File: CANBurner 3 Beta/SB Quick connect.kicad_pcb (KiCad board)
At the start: 2 copper layers, 33.8 x 30 mm, 9 parts

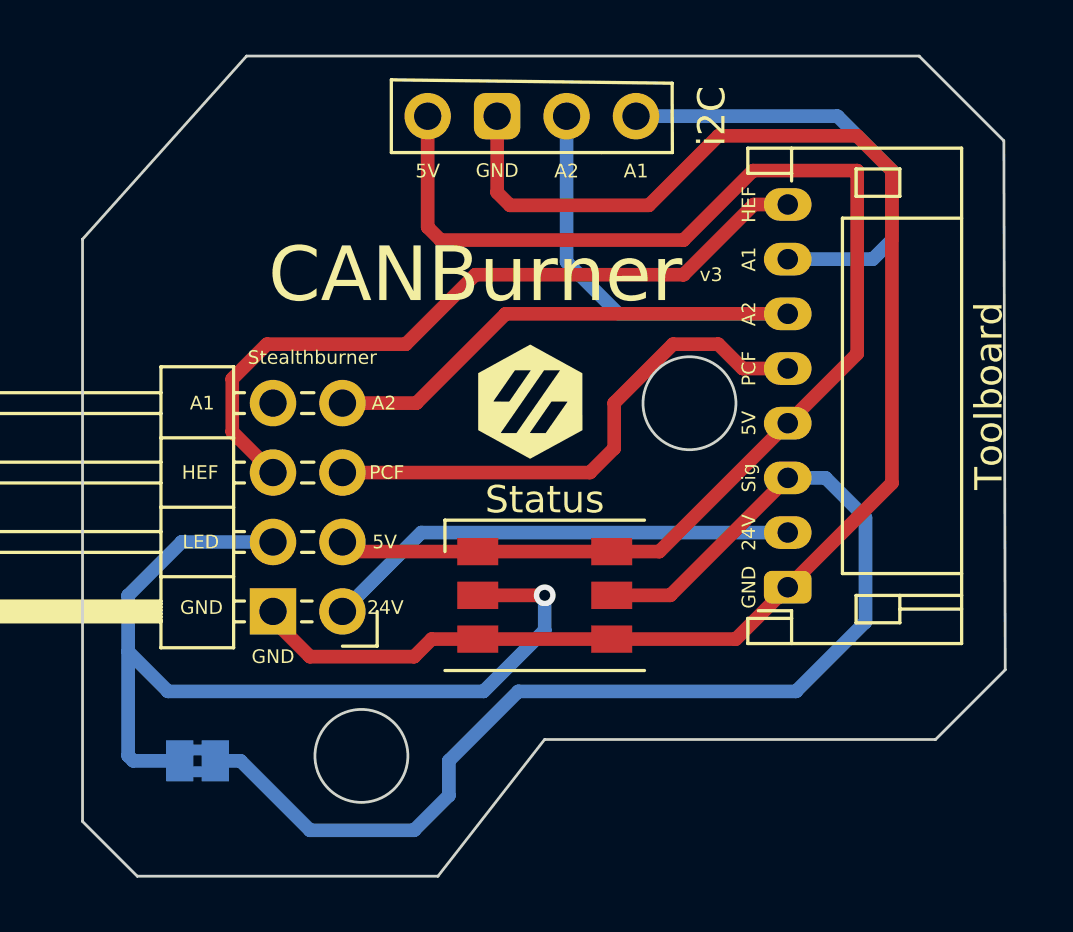
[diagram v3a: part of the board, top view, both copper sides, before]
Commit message: v3 Fixes 🪲⚡
Added missing track for A1.
Moved PCF track further from mounting hole.
Used correct footprint for LED bypass.
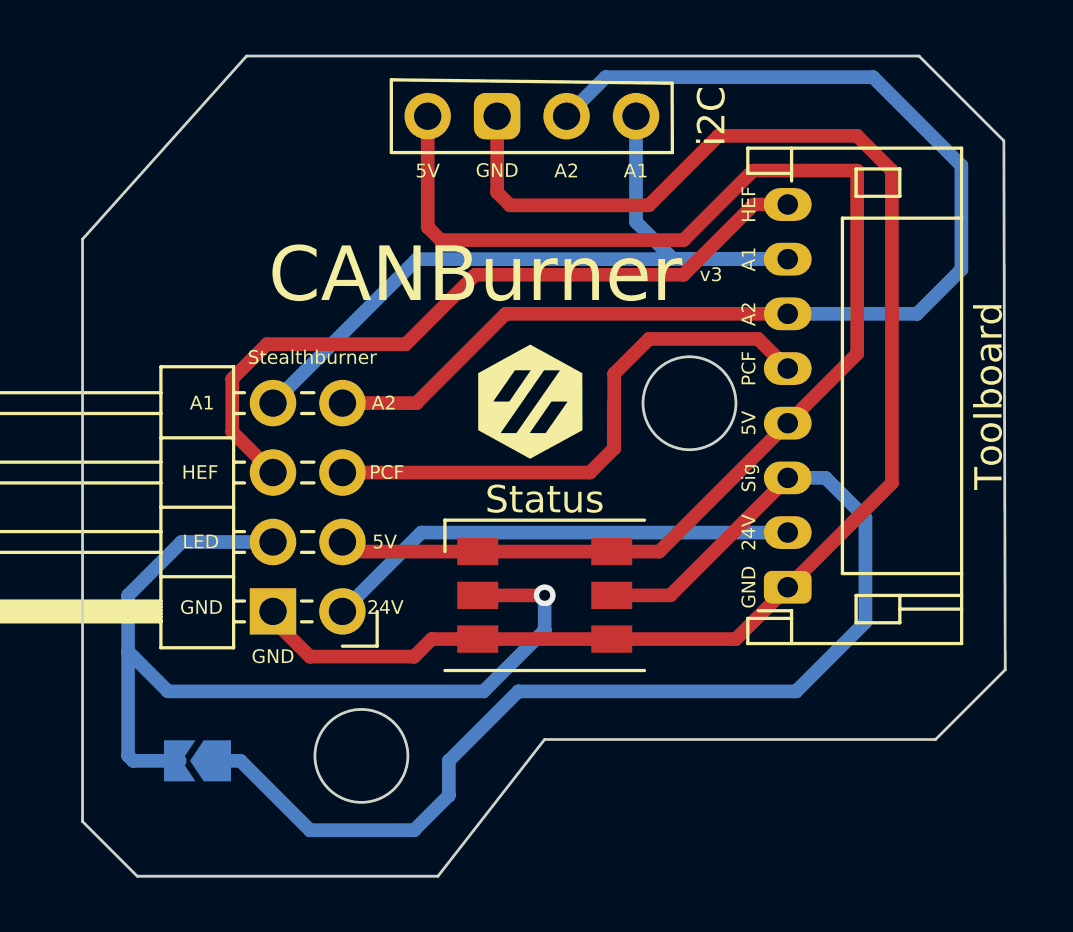
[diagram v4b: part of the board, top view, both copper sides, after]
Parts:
- LED Bypass: footprint Jumper:SolderJumper-2_P1.3mm_Bridged2Bar_Pad1.0x1.5mm -> Jumper:SolderJumper-2_P1.3mm_Open_TrianglePad1.0x1.5mm
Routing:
- net /A1: track 16.8 -> 31.0 mm
- net /A2: track 31.8 -> 44.8 mm
- net /PCF: track 19.6 -> 22.0 mm
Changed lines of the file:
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@@
       ) (layer "B.SilkS") (width 0) (fill solid))
   )
-  (footprint "Jumper:SolderJumper-2_P1.3mm_Bridged2Bar_Pad1.0x1.5mm" (layer "B.Cu")
+  (footprint "Jumper:SolderJumper-2_P1.3mm_Open_TrianglePad1.0x1.5mm" (layer "B.Cu")
     (at 68.58 45.91 180)
-    (descr "SMD Solder Jumper, 1x1.5mm Pads, 0.3mm gap, bridged with 2 copper strips")
-    (tags "net tie solder jumper bridged")
+    (descr "SMD Solder Jumper, 1x1.5mm Triangular Pads, 0.3mm gap, open")
+    (tags "solder jumper open")
     (attr exclude_from_pos_files exclude_from_bom)
     (fp_text reference "LED Bypass" (at 0 1.8) (layer "B.SilkS")
-      (effects (font (size 0.5 0.5) (thickness 0.15)) (justify mirror))
+      (effects (font (size 0.5 0.5) (thickness 0.1)) (justify mirror))
     )
-    (fp_text value "LED Bypass" (at 0 -1.9) (layer "B.Fab") hide
-      (effects (font (size 0.5 0.5) (thickness 0.15)) (justify mirror))
+    (fp_text value "LED Bypass" (at 0 -1.9) (layer "B.Fab")
+      (effects (font (size 1 1) (thickness 0.15)) (justify mirror))
     )
-    (fp_poly (pts
-        (xy -0.25 -0.2)
-        (xy 0.25 -0.2)
-        (xy 0.25 -0.6)
-        (xy -0.25 -0.6)
-      ) (layer "B.Cu") (width 0) (fill solid))
-    (fp_poly (pts
-        (xy -0.25 0.6)
-        (xy 0.25 0.6)
-        (xy 0.25 0.2)
-        (xy -0.25 0.2)
-      ) (layer "B.Cu") (width 0) (fill solid))
+    (fp_line (start 1.4 -1) (end -1.4 -1) (layer "B.SilkS") (width 0.12))
     (fp_line (start -1.4 1) (end 1.4 1) (layer "B.SilkS") (width 0.12))
     (fp_line (start 1.4 1) (end 1.4 -1) (layer "B.SilkS") (width 0.12))
     (fp_line (start -1.4 -1) (end -1.4 1) (layer "B.SilkS") (width 0.12))
-    (fp_line (start 1.4 -1) (end -1.4 -1) (layer "B.SilkS") (width 0.12))
     (fp_line (start 1.65 -1.25) (end -1.65 -1.25) (layer "B.CrtYd") (width 0.05))
     (fp_line (start -1.65 1.25) (end -1.65 -1.25) (layer "B.CrtYd") (width 0.05))
     (fp_line (start 1.65 -1.25) (end 1.65 1.25) (layer "B.CrtYd") (width 0.05))
     (fp_line (start -1.65 1.25) (end 1.65 1.25) (layer "B.CrtYd") (width 0.05))
-    (pad "1" smd rect (at -0.65 0 180) (size 1 1.5) (layers "B.Cu" "B.Mask")
-      (net 6 "/Sig"))
-    (pad "2" smd rect (at 0.65 0 180) (size 1 1.5) (layers "B.Cu" "B.Mask")
-      (net 6 "/Sig"))
+    (pad "1" smd custom (at -0.725 0 180) (size 0.3 0.3) (layers "B.Cu" "B.Mask")
+      (net 6 "/Sig") (zone_connect 2)
+      (options (clearance outline) (anchor rect))
+      (primitives
+        (gr_poly (pts
+            (xy 1 0)
+            (xy 0.5 -0.75)
+            (xy -0.5 -0.75)
+            (xy -0.5 0.75)
+            (xy 0.5 0.75)
+          ) (width 0) (fill yes))
+      ))
+    (pad "2" smd custom (at 0.725 0 180) (size 0.3 0.3) (layers "B.Cu" "B.Mask")
+      (net 6 "/Sig") (zone_connect 2)
+      (options (clearance outline) (anchor rect))
+      (primitives
+        (gr_poly (pts
+            (xy 0.5 -0.75)
+            (xy -0.65 -0.75)
+            (xy -0.15 0)
+            (xy -0.65 0.75)
+            (xy 0.5 0.75)
+          ) (width 0) (fill yes))
+      ))
   )
   (footprint "LOGO" (layer "B.Cu")
@@
   (segment (start 76.2 30.67) (end 71.12 30.67) (width 0.5) (layer "F.Cu") (net 2))
   (segment (start 71.12 30.67) (end 69.85 31.94) (width 0.5) (layer "F.Cu") (net 2))
-  (segment (start 91.990407 22.330407) (end 84.619469 22.330407) (width 0.5) (layer "B.Cu") (net 3))
-  (segment (start 93.28 27.56) (end 93.98 26.86) (width 0.5) (layer "B.Cu") (net 3))
-  (segment (start 93.98 26.86) (end 93.98 24.32) (width 0.5) (layer "B.Cu") (net 3))
-  (segment (start 90.17 27.56) (end 93.28 27.56) (width 0.5) (layer "B.Cu") (net 3))
-  (segment (start 93.98 24.32) (end 91.990407 22.330407) (width 0.5) (layer "B.Cu") (net 3))
+  (segment (start 90.17 27.56) (end 85.98 27.56) (width 0.5) (layer "B.Cu") (net 3))
+  (segment (start 84.619469 26.199469) (end 84.619469 22.330407) (width 0.5) (layer "B.Cu") (net 3))
+  (segment (start 85.98 27.56) (end 84.619469 26.199469) (width 0.5) (layer "B.Cu") (net 3))
+  (segment (start 76.606341 27.56) (end 71.341315 32.825026) (width 0.5) (layer "B.Cu") (net 3))
+  (segment (start 90.17 27.56) (end 76.606341 27.56) (width 0.5) (layer "B.Cu") (net 3))
   (segment (start 90.17 29.56) (end 79.85 29.56) (width 0.5) (layer "F.Cu") (net 4))
   (segment (start 79.85 29.56) (end 76.584974 32.825026) (width 0.5) (layer "F.Cu") (net 4))
   (segment (start 76.584974 32.825026) (end 73.881315 32.825026) (width 0.5) (layer "F.Cu") (net 4))
-  (segment (start 82.079469 27.659469) (end 82.079469 22.330407) (width 0.5) (layer "B.Cu") (net 4))
-  (segment (start 90.17 29.56) (end 83.98 29.56) (width 0.5) (layer "B.Cu") (net 4))
-  (segment (start 83.98 29.56) (end 82.079469 27.659469) (width 0.5) (layer "B.Cu") (net 4))
-  (segment (start 90.17 31.56) (end 88.52 31.56) (width 0.5) (layer "F.Cu") (net 5))
-  (segment (start 88.52 31.56) (end 87.63 30.67) (width 0.5) (layer "F.Cu") (net 5))
+  (segment (start 90.17 29.56) (end 94.9 29.56) (width 0.5) (layer "B.Cu") (net 4))
+  (segment (start 83.50708 20.902796) (end 82.079469 22.330407) (width 0.5) (layer "B.Cu") (net 4))
+  (segment (start 93.292796 20.902796) (end 83.50708 20.902796) (width 0.5) (layer "B.Cu") (net 4))
+  (segment (start 94.9 29.56) (end 96.52 27.94) (width 0.5) (layer "B.Cu") (net 4))
+  (segment (start 96.52 24.13) (end 93.292796 20.902796) (width 0.5) (layer "B.Cu") (net 4))
+  (segment (start 96.52 27.94) (end 96.52 24.13) (width 0.5) (layer "B.Cu") (net 4))
   (segment (start 82.934974 35.365026) (end 73.881315 35.365026) (width 0.5) (layer "F.Cu") (net 5))
+  (segment (start 83.82 31.75) (end 83.82 33.02) (width 0.5) (layer "F.Cu") (net 5))
   (segment (start 83.82 32.822549) (end 83.82 34.48) (width 0.5) (layer "F.Cu") (net 5))
+  (segment (start 90.17 31.56) (end 89.09 30.48) (width 0.5) (layer "F.Cu") (net 5))
+  (segment (start 85.09 30.48) (end 83.82 31.75) (width 0.5) (layer "F.Cu") (net 5))
+  (segment (start 89.09 30.48) (end 85.09 30.48) (width 0.5) (layer "F.Cu") (net 5))
   (segment (start 83.82 34.48) (end 82.934974 35.365026) (width 0.5) (layer "F.Cu") (net 5))
-  (segment (start 87.63 30.67) (end 85.972549 30.67) (width 0.5) (layer "F.Cu") (net 5))
-  (segment (start 85.972549 30.67) (end 83.82 32.822549) (width 0.5) (layer "F.Cu") (net 5))
+  (segment (start 83.82 33.02) (end 83.82 34.48) (width 0.5) (layer "F.Cu") (net 5))
   (segment (start 90.17 35.56) (end 85.873186 39.856814) (width 0.5) (layer "F.Cu") (net 6))
   (segment (start 78.83 39.856814) (end 81.28 39.856814) (width 0.5) (layer "F.Cu") (net 6))
